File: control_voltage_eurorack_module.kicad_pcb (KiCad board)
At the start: 2 copper layers, 71.1 x 110 mm, 50 parts, among them J1 Conn_02x08_Odd_Even, J2 AVR-ISP-6, J3 CVOut, J4 Conn_01x04, J5 ExtClkIn, J6 TrigOut, J7 GateOut, SW1 Menu_Encoder, U1 TL072, U2 ATmega16-16AU, U3 MCP4725xxx-xCH, Y1 16M

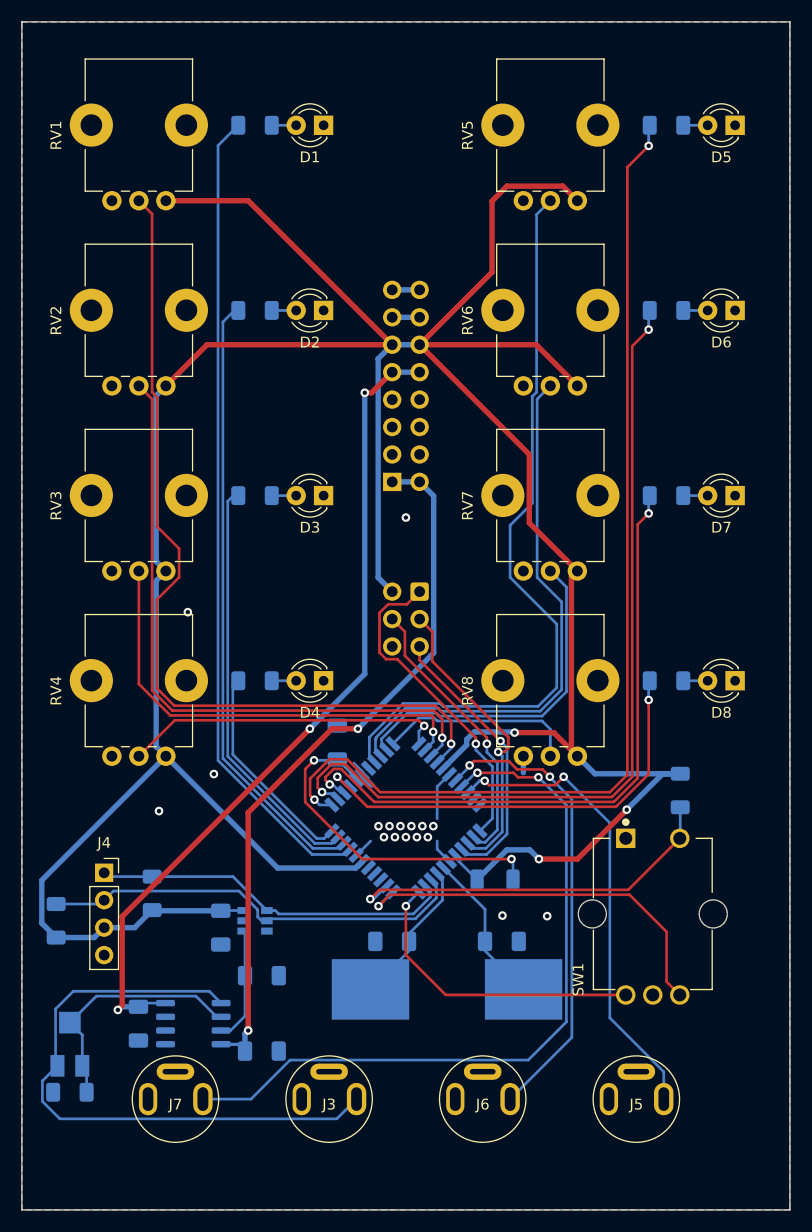
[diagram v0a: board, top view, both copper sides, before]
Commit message: fixed wrong i2c pins and added uart port
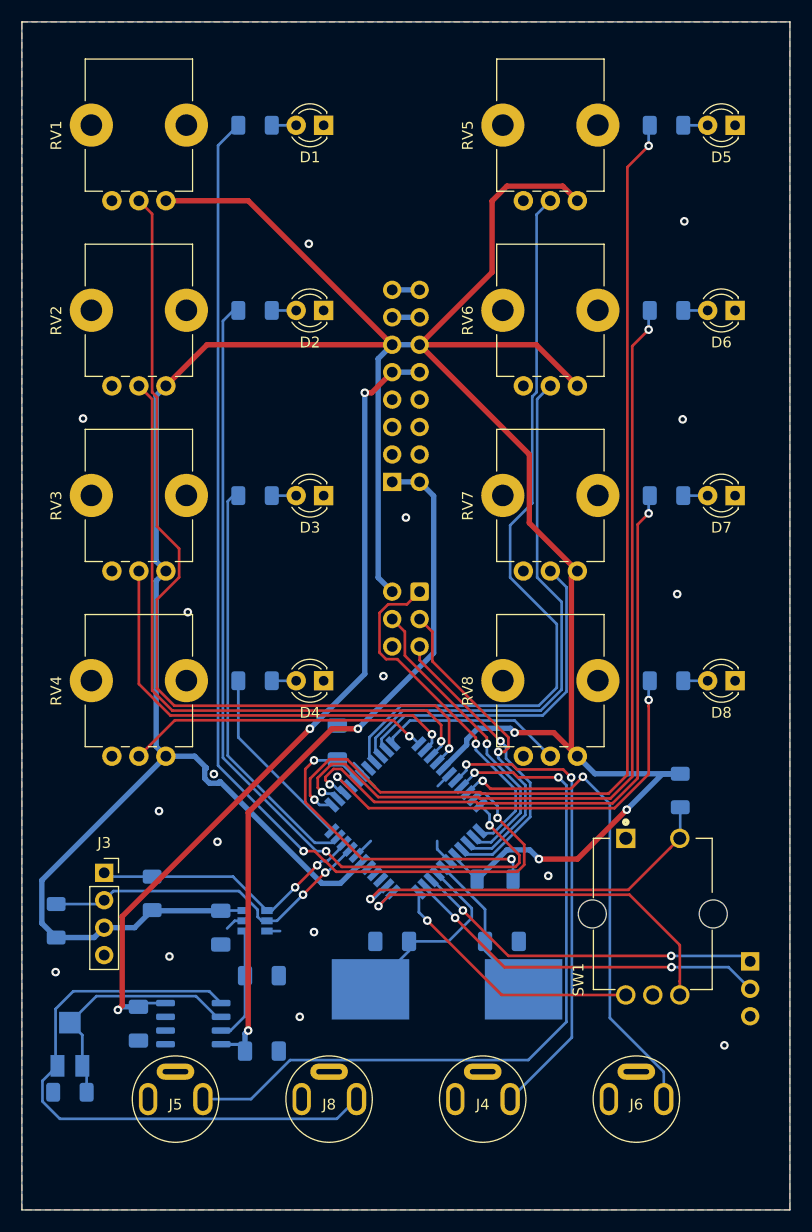
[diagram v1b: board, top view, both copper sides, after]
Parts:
- added J7: Conn_01x03, Connector_PinHeader_2.54mm:PinHeader_1x03_P2.54mm_Vertical, B.Cu at (82.0, 102.2)
- U2: value ATmega16-16AU -> ATmega16A-AU
- renumbered C3 to C1, C7 to C2, C1 to C3, C2 to C4, C4 to C5, C5 to C6, C8 to C7, J4 to J3, J6 to J4, J7 to J5, J5 to J6, J3 to J8, R9 to R10, R10 to R11, R11 to R12, R12 to R9, RV10 to RV9
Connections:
- U2 pad 10: SDA -> TXD
- U2 pad 14: (no net) -> Net-(U2-Pad14)
- U2 pad 15: (no net) -> Net-(U2-Pad15)
- U2 pad 16: (no net) -> Net-(U2-Pad16)
- U2 pad 19: LED0 -> SCL
- U2 pad 20: LED1 -> SDA
- U2 pad 29: (no net) -> Net-(U2-Pad29)
- U2 pad 43: (no net) -> LED0
- U2 pad 44: (no net) -> LED1
- U2 pad 9: SCL -> RXD
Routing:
- net TXD: track 0.00 -> 34.2 mm, vias 0 -> 2
- net RXD: track 0.00 -> 32.7 mm, vias 0 -> 2
- net LED0: track 75.6 -> 102.1 mm, vias 0 -> 2
- net LED1: track 56.7 -> 80.5 mm, vias 0 -> 2
- net SCL: track 40.0 -> 32.7 mm, vias 0 -> 2
- net SDA: track 34.1 -> 27.5 mm, vias 0 -> 2
- net Net-(C3-Pad1): track 16.0 -> 20.4 mm
- net Net-(SW1-PadA): track 28.2 -> 24.2 mm
- net MISO: track 30.1 -> 32.9 mm
- net +5V: track 312.3 -> 314.7 mm
- net LED3: track 19.7 -> 17.5 mm
- net Rst: track 25.9 -> 28.0 mm
- net SCK: track 28.0 -> 30.1 mm
- net MOSI: track 26.4 -> 28.5 mm
- net Pot3: track 29.9 -> 28.2 mm
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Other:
- board text added: "GND"
- board text added: "RX"
- board text added: "TX"
